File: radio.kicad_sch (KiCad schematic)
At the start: 49 parts, among them U11 MAX5865

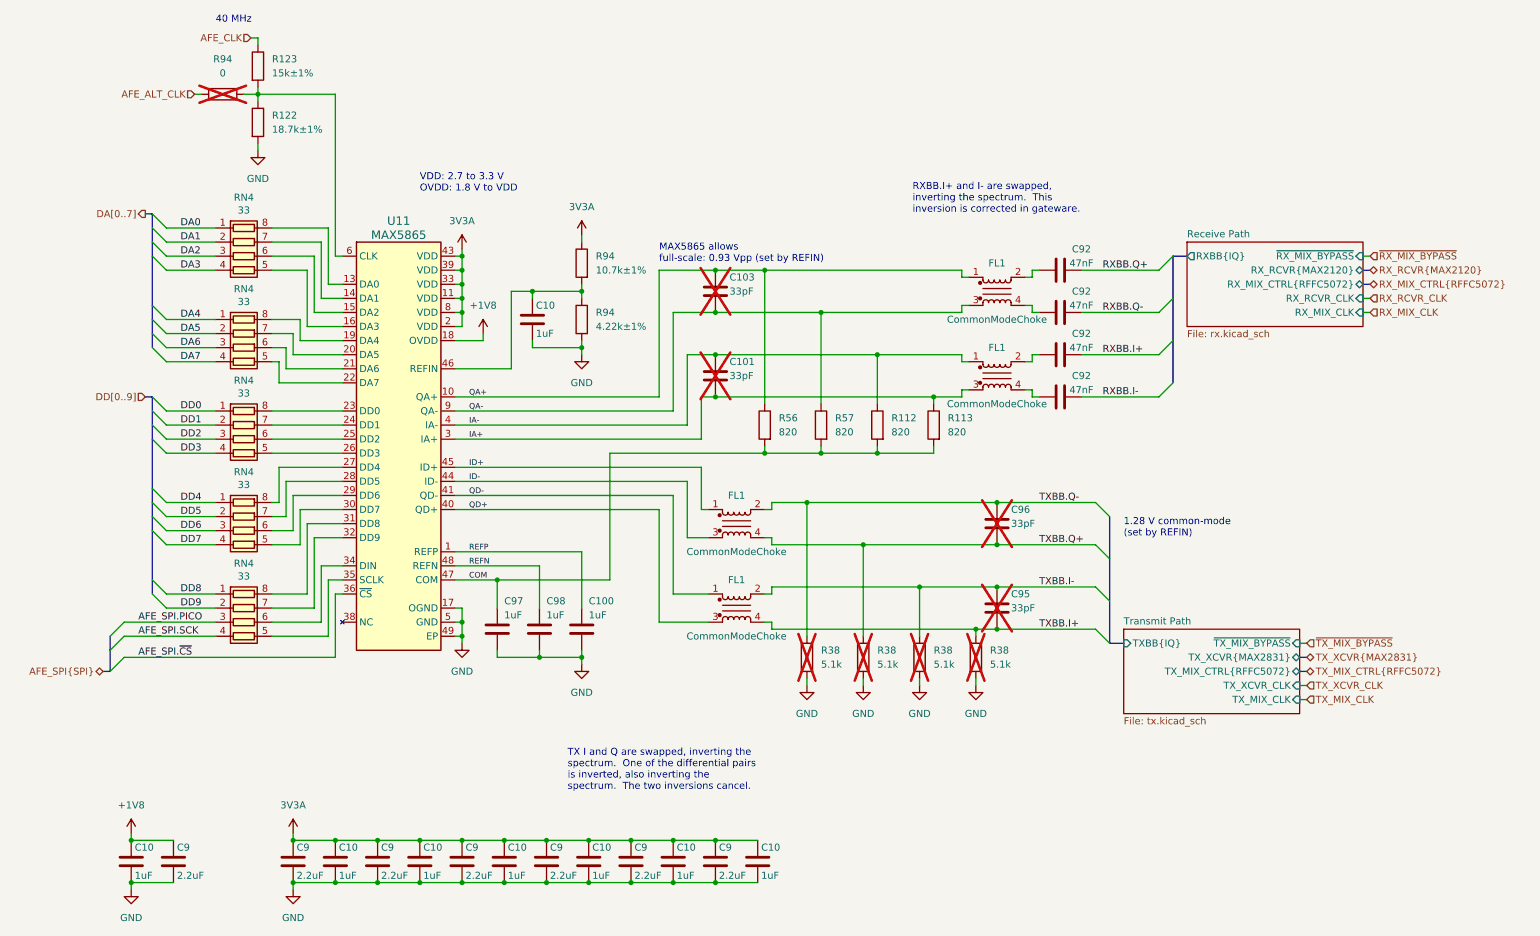
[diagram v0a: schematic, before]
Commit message: Replace open drain clock inverters with push-pull
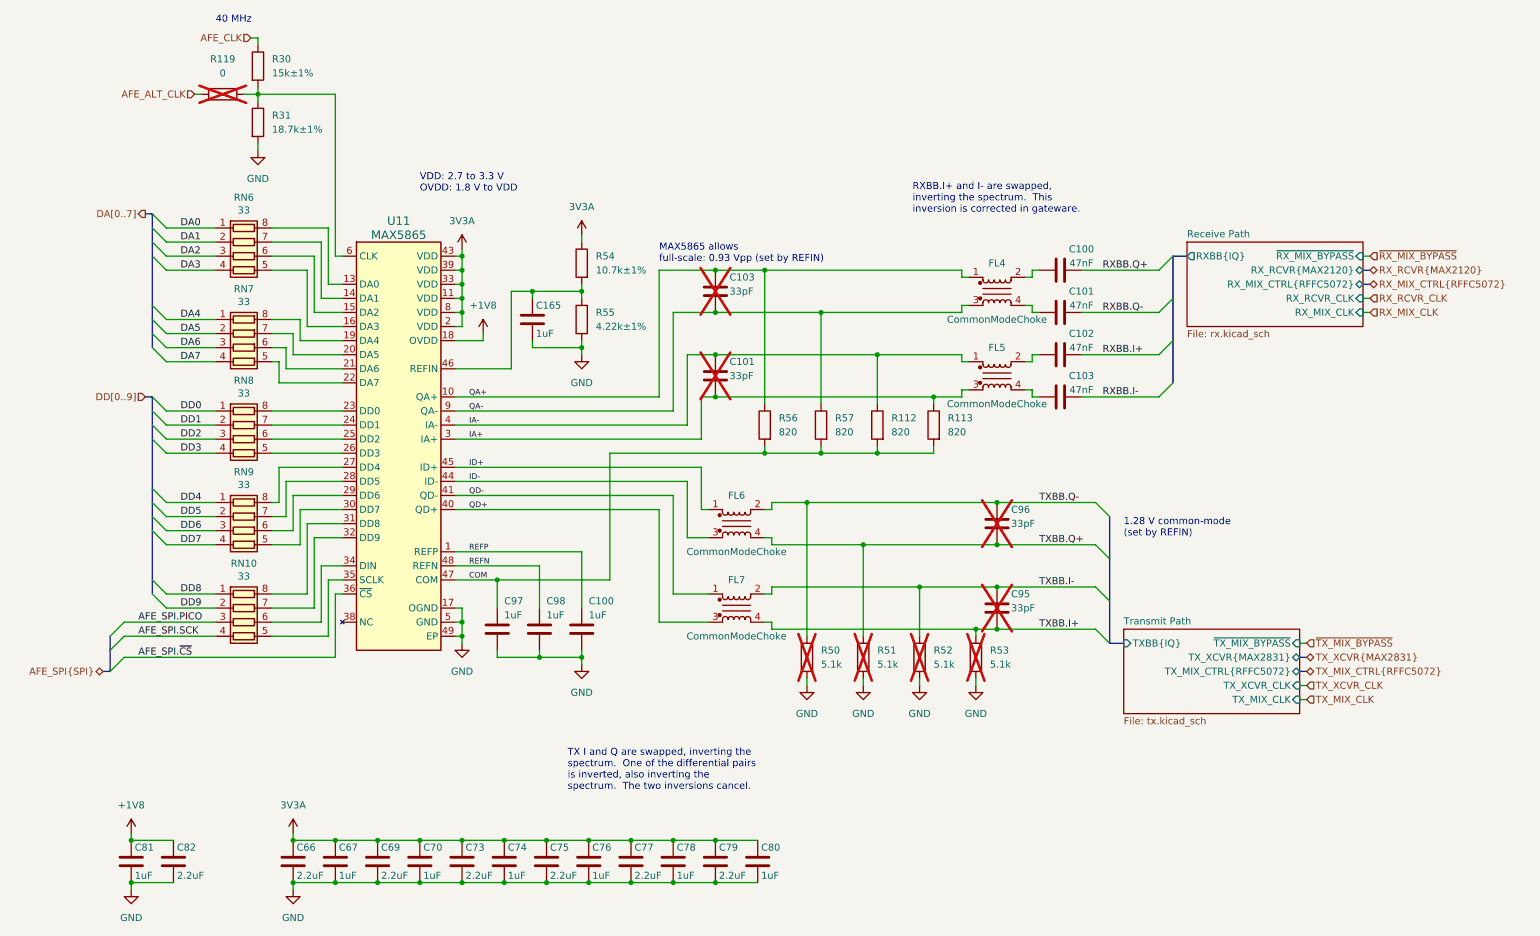
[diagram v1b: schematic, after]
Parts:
- renumbered C92 to C100, C92 to C101, C92 to C102, C92 to C103, C10 to C165, C9 to C66, C10 to C67, C9 to C69, C10 to C70, C9 to C73, C10 to C74, C9 to C75, C10 to C76, C9 to C77, C10 to C78, C9 to C79, C10 to C80, C10 to C81, C9 to C82, FL1 to FL4, FL1 to FL5, FL1 to FL6, FL1 to FL7, R94 to R119, R123 to R30, R122 to R31, R38 to R50, R38 to R51, R38 to R52, R38 to R53, R94 to R54, R94 to R55, RN4 to RN10, RN4 to RN6, RN4 to RN7, RN4 to RN8, RN4 to RN9

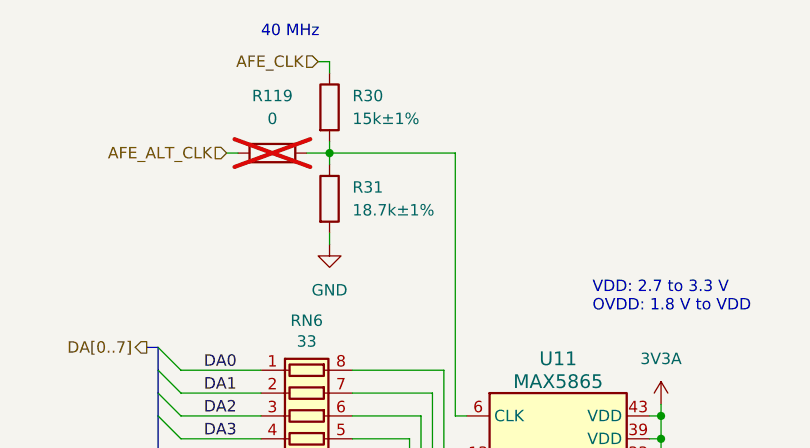
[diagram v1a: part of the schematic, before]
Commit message: Tune clock passives
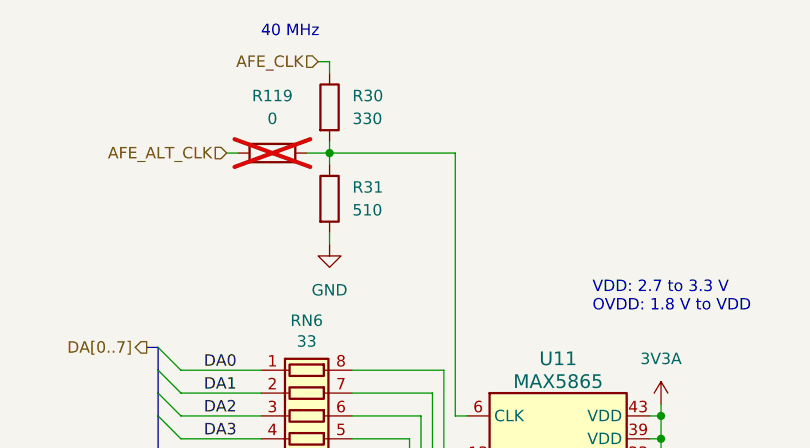
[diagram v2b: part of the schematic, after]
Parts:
- R30: value 15k±1% -> 330; Part Number RC0402FR-0715KL -> RC0402FR-13330RL
- R31: value 18.7k±1% -> 510; Manufacturer Panasonic -> Yageo; Part Number ERJ-2RKF1872X -> RC0402FR-07510RL
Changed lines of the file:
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@@
       (effects (font (size 1.27 1.27)) (justify left))
     )
-    (property "Value" "18.7k±1%" (at 59.69 41.91 0)
+    (property "Value" "510" (at 59.69 41.91 0)
       (effects (font (size 1.27 1.27)) (justify left))
     )
@@
       (effects (font (size 1.27 1.27)) hide)
     )
-    (property "Description" "RES SMD 18.7K OHM 1% 1/10W 0402" (at 57.15 40.64 0)
-      (effects (font (size 1.27 1.27)) hide)
-    )
-    (property "Manufacturer" "Panasonic" (at 57.15 40.64 0)
-      (effects (font (size 1.27 1.27)) hide)
-    )
-    (property "Part Number" "ERJ-2RKF1872X" (at 57.15 40.64 0)
+    (property "Description" "RES 510 OHM 1% 1/16W 0402" (at 57.15 40.64 0)
+      (effects (font (size 1.27 1.27)) hide)
+    )
+    (property "Manufacturer" "Yageo" (at 57.15 40.64 0)
+      (effects (font (size 1.27 1.27)) hide)
+    )
+    (property "Part Number" "RC0402FR-07510RL" (at 57.15 40.64 0)
       (effects (font (size 1.27 1.27)) hide)
     )
@@
       (effects (font (size 1.27 1.27)) (justify left))
     )
-    (property "Value" "15k±1%" (at 59.69 31.75 0)
+    (property "Value" "330" (at 59.69 31.75 0)
       (effects (font (size 1.27 1.27)) (justify left))
     )
@@
       (effects (font (size 1.27 1.27)) hide)
     )
-    (property "Part Number" "RC0402FR-0715KL" (at 57.15 30.48 0)
+    (property "Part Number" "RC0402FR-13330RL" (at 57.15 30.48 0)
       (effects (font (size 1.27 1.27)) hide)
     )
@@
       (effects (font (size 1.27 1.27)) hide)
     )
-    (property "Description" "RES 15K OHM 1% 1/16W 0402" (at 57.15 30.48 0)
-      (effects (font (size 1.27 1.27)) hide)
-    )
+    (property "Description" "RES 330 OHM 1% 1/16W 0402" (at 57.15 30.48 0)
+      (effects (font (size 1.27 1.27)) hide)
+    )
